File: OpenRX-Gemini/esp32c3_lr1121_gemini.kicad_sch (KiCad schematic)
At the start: 60 parts, among them T1 0900PC16J0042001E, U1 ESP32-C3FH4, U10 RFX2401C, U2 TLV75533PDQNR, U4 LR1121IMLTRT, U5 OW7EL89CENUYO3YLC-32M, U8 OW7EL89CENUYO3YLC-32M, U9 LR1121IMLTRT, X1 CJ17-400001010B20

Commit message: Gemini: copy Mono schematic as base for dual-radio build
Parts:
- removed C35, C36, C37, C40: 100nF, Capacitor_SMD:C_0201_0603Metric, symbol Device:C
- removed C38: 10pF, Capacitor_SMD:C_0201_0603Metric, symbol Device:C
- removed C39: 4.7uF, Capacitor_SMD:C_0402_1005Metric, symbol Device:C
- removed C41: 220pF, Capacitor_SMD:C_0201_0603Metric, symbol Device:C
- removed C42: 1uF, Capacitor_SMD:C_0201_0603Metric, symbol Device:C
- removed JP3: U.FL-R-SMT-1(80), OpenRX-Shared:RF-SMD_FRF05002-JSS103M, symbol OpenRX-Shared:U.FL-R-SMT-1(80)
- removed L4: 10uH, Inductor_SMD:L_0603_1608Metric, symbol Device:L
- removed R12: 220R, Resistor_SMD:R_0201_0603Metric, symbol Device:R
- removed R13, R14, R15, R16, R5, R7: 100k, Resistor_SMD:R_0201_0603Metric, symbol Device:R
- removed R8: 10k, Resistor_SMD:R_0201_0603Metric, symbol Device:R
- removed U10: RFX2401C, OpenRX-Shared:QFN-16_L3.0-W3.0-P0.50-BL-EP1.7, symbol OpenRX-Shared:RFX2401C
- removed U8: OW7EL89CENUYO3YLC-32M, OpenRX-Shared:OSC-SMD_4P-L2.0-W1.6-BL_TXC_7Z, symbol OpenRX-Shared:OW7EL89CENUYO3YLC-32M
- removed U9: LR1121IMLTRT, OpenRX-Shared:QFN-32_L5.0-W5.0-P0.50-BL-EP3.7, symbol OpenRX-Shared:LR1121IMLTRT
- added C14: 1uF, Capacitor_SMD:C_0201_0603Metric, symbol Device:C
- added C15: 220pF, Capacitor_SMD:C_0201_0603Metric, symbol Device:C
- added C16: 0.3pF, Capacitor_SMD:C_0201_0603Metric, symbol Device:C
- added C17: 100pF, Capacitor_SMD:C_0201_0603Metric, symbol Device:C
- added C18: 100nF, Capacitor_SMD:C_0201_0603Metric, symbol Device:C
- added D1: XL-1010RGBC-WS2812B, OpenRX-Shared:LED-SMD_4P-L1.0-W1.0-TL_XL-1010RGBC-WS2812B, symbol OpenRX-Shared:XL-1010RGBC-WS2812B
- added U3: TS2306A 240GF MSM 9_C2976675, OpenRX-Shared:SW-SMD_4P-L3.0-W2.0-P0.85-LS3.5, symbol OpenRX-Shared:TS2306A240GFMSM9_C2976675
- added U6: SKY13588-460LF, OpenRX-Shared:QFN-12_L2.0-W2.0-P0.50-BL-EP0.8, symbol OpenRX-Shared:SKY13588-460LF
- added U7: RFX2401C, OpenRX-Shared:QFN-16_L3.0-W3.0-P0.50-BL-EP1.7, symbol OpenRX-Shared:RFX2401C
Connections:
- net +3V3: now also C14.1, C15.1, U6.6 (VDD), U7.14 (VDD), U7.16 (VDD)
- net +5V: now also C18.1, D1.2 (VDD)
- net GND: now also C23.1, C14.2, C15.2, C16.2, C18.2, D1.3 (GND), U3.2, U6.10 (GND), U6.12 (GND), U6.13 (EP), U6.2 (GND), U6.7 (GND), U6.8 (GND), U7.1 (GND), U7.11 (GND), U7.12 (GND), U7.15 (GND), U7.17 (EP), U7.2 (GND), U7.3 (GND), U7.7 (GND), U7.8 (GND), U7.9 (GND)
- net MISO: now also U1.10 (MTDI); no longer U1.12 (MTCK)
- net MOSI: now also U1.9 (MTMS); no longer U1.13 (MTDO)
- net RXEN: now also U4.20 (DIO5), U7.6 (RXEN)
- net SCK: now also U1.12 (MTCK); no longer U1.9 (MTMS)
- net TXEN: now also U4.19 (DIO6), U7.5 (TXEN)
- net DIO8-1: now reaches U4.10 (DIO8)
- net DIO8-1: now also U6.5 (V2)
- net at USB2.1 (IN): now also U4.26 (RFIO_HF)
- net at USB2.3 (OUT): now also U7.4 (TXRX)
- net DIO7-1: now reaches U4.11 (DIO7)
- net DIO7-1: now also U6.4 (V1)
- net at U5.4 (VDD): now also C23.2, U4.3 (VTCXO); no longer C23.1
- net at T1.6 (RX), T1.8 (TX_LP), T1.9 (TX_HP): now also U6.1 (J1); no longer JP1.1 (SIG)
- net BUSY renamed BUSY1
- net BUSY2 renamed IRQ1
- net IRQ1: now also U4.9 (DIO9)
- removed net DIO1: U1.10 (MTDI), U4.9 (DIO9)
- net IRQ renamed BUTTON
- net BUTTON: now also U3.1
- net NSS renamed NSS1
- net NSS1: now also U1.13 (MTDO); no longer U1.14 (GPIO8)
- net NSS2: no longer names the net of U1.16 (GPIO10)
- net RST renamed RST1
- net RST2: no longer names the net of U1.4 (XTAL_32K_P)
- new net: C16.1, C17.2, U7.10 (ANT)
- new net: JP1.1 (SIG), U6.11 (RFC)
- new net: C17.1, U6.9 (J2)
- new net LED: D1.4 (DIN), U1.14 (GPIO8)
- no-connect marks 31 -> 22
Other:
- note removed: "interrupt (naming from lite/nano)"

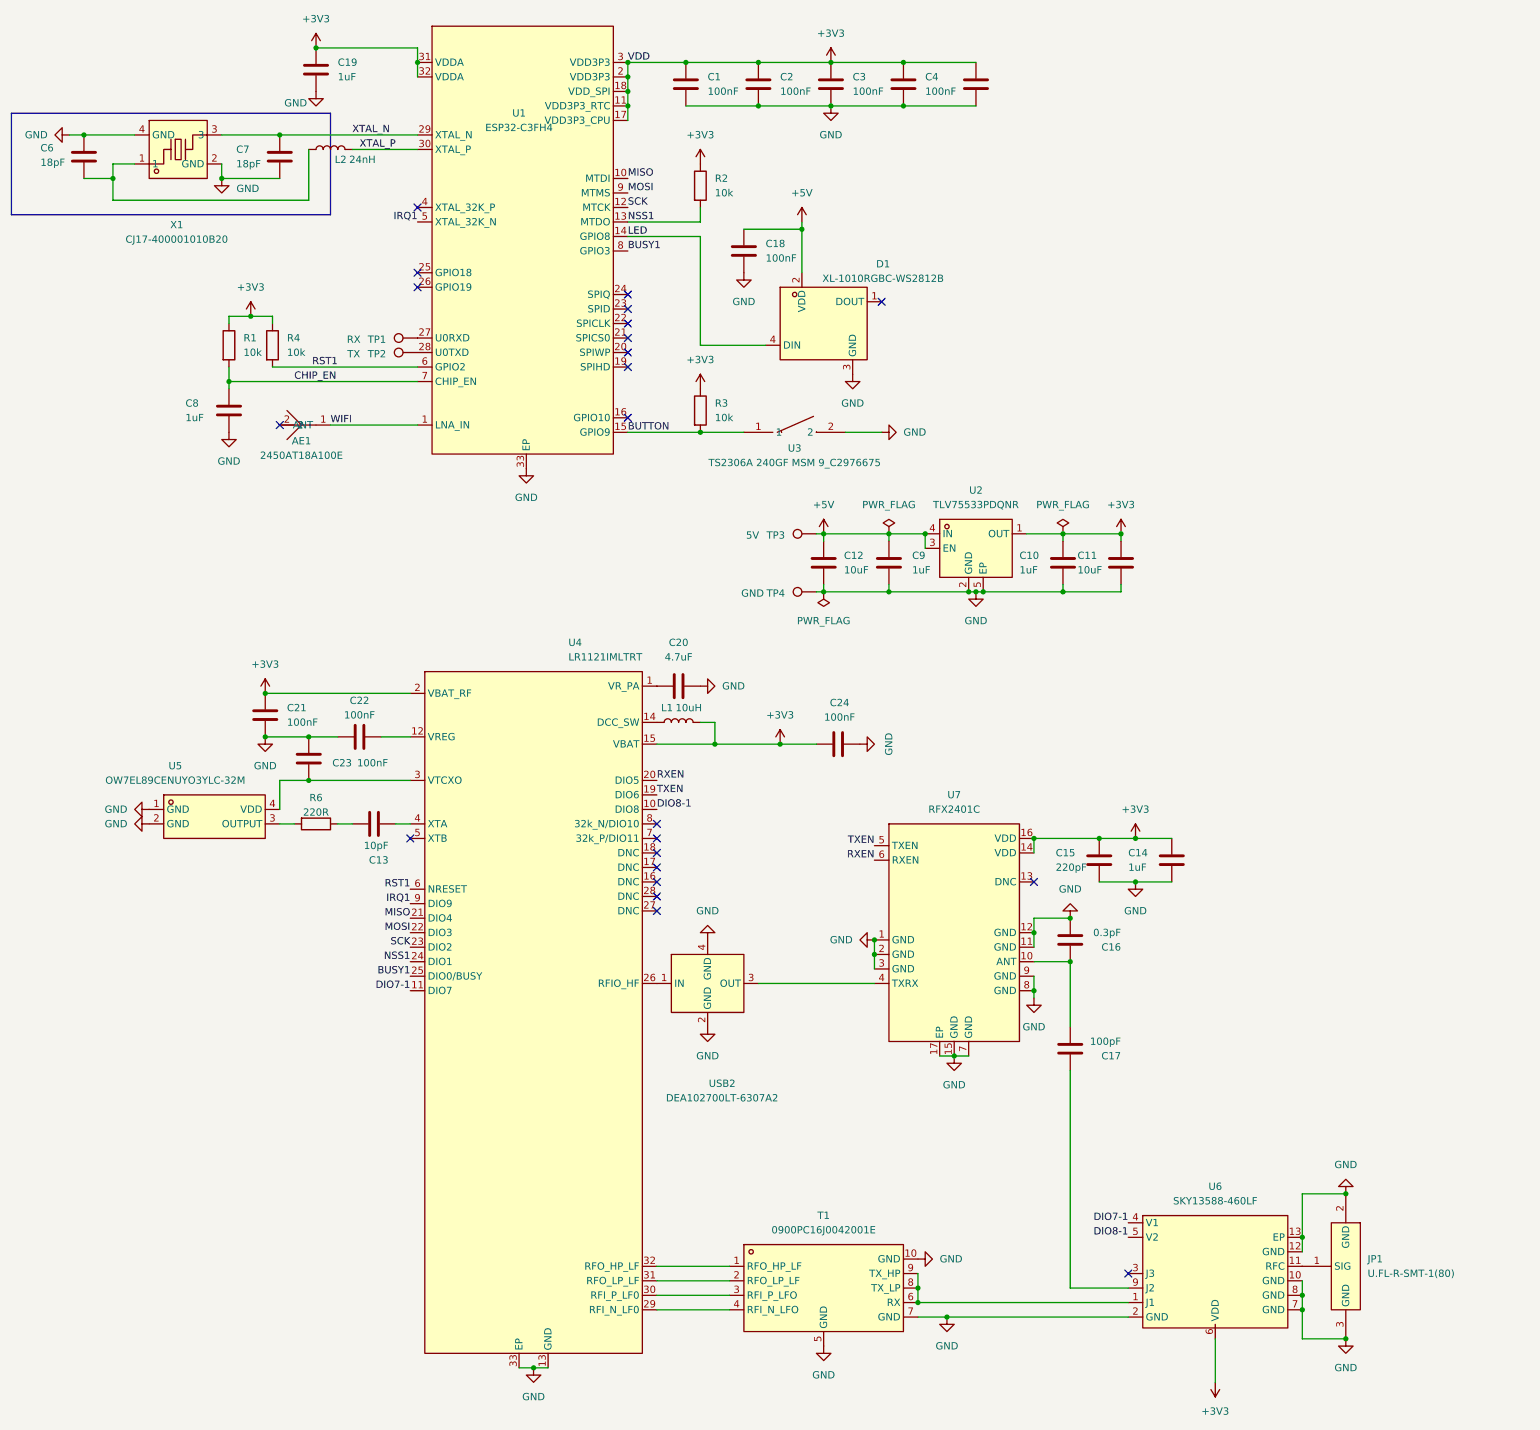
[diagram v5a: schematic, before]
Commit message: Gemini: copy Mono schematic + PCB as starting point
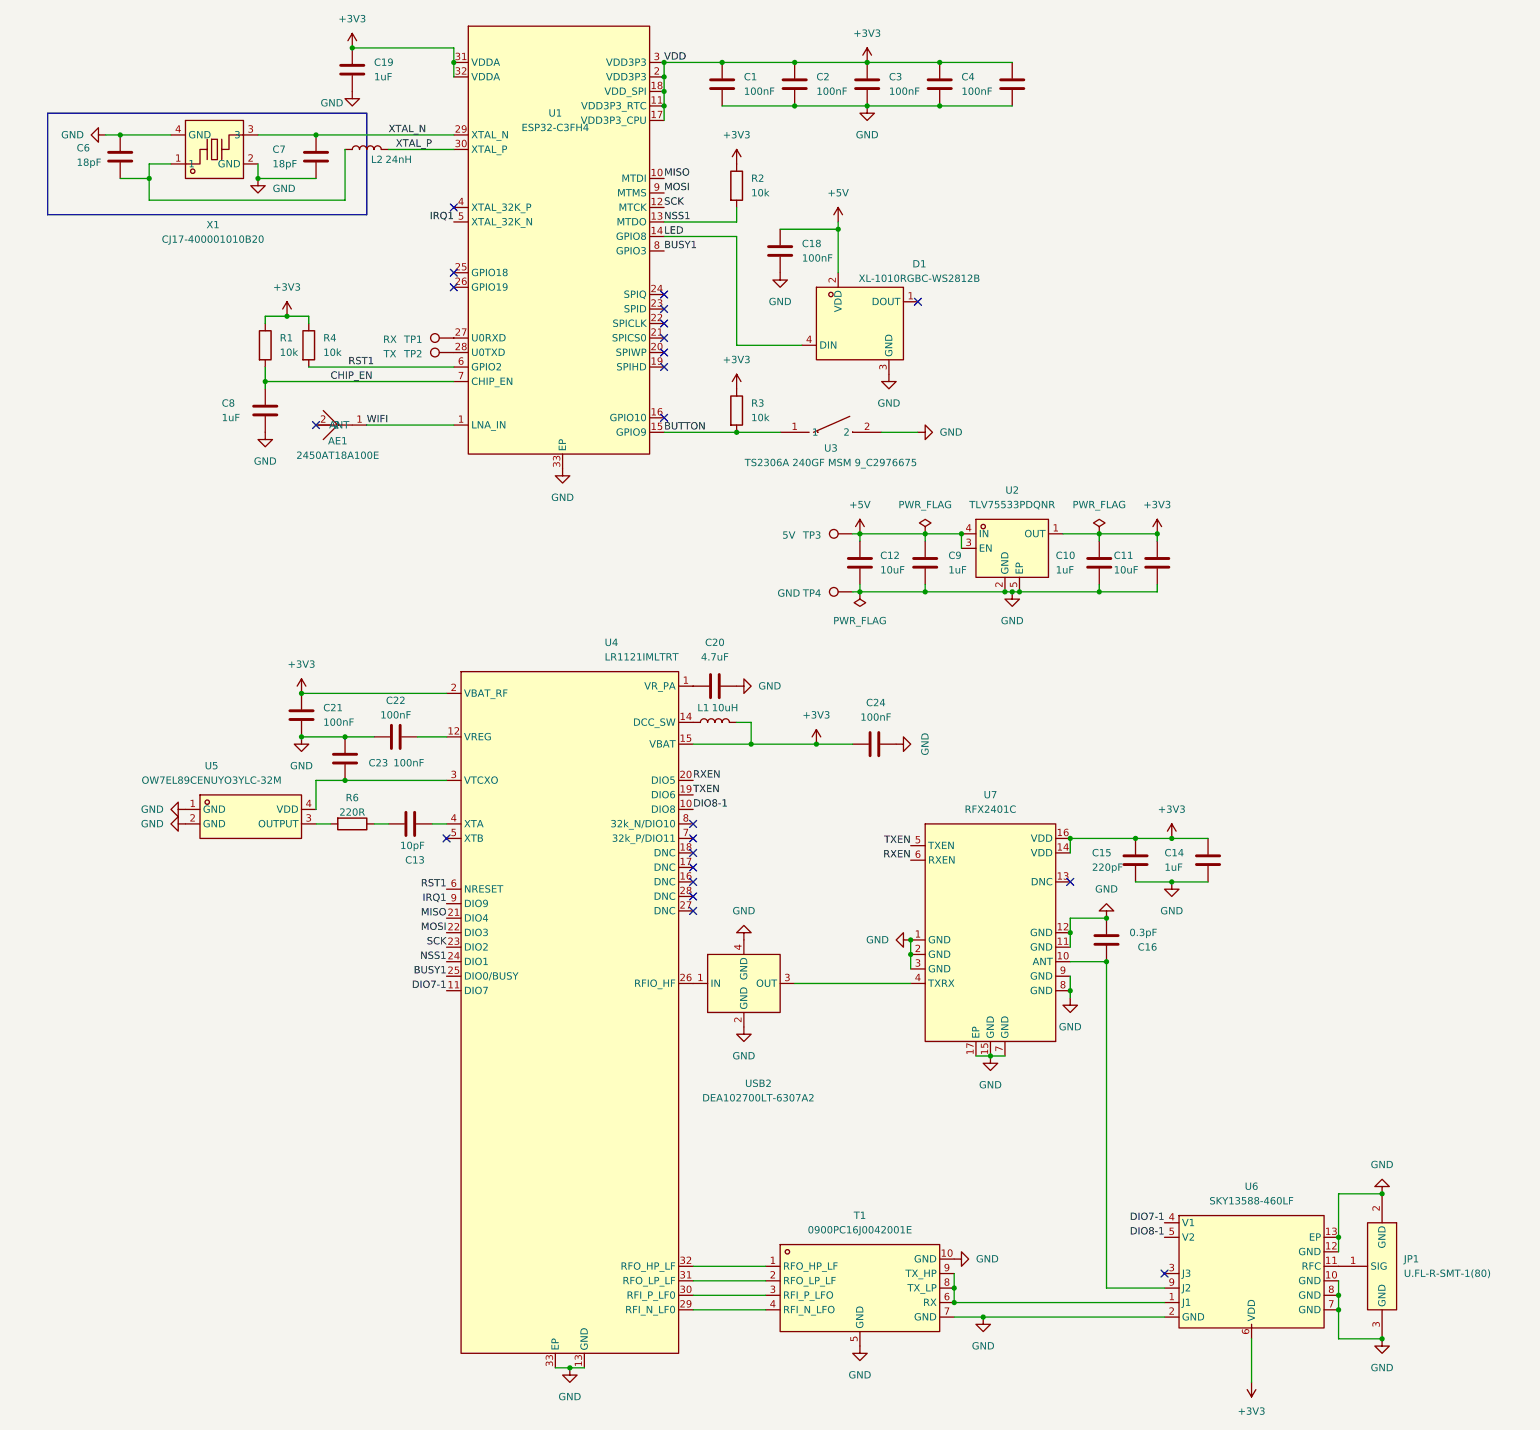
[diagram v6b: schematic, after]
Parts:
- removed C17: 100pF, Capacitor_SMD:C_0201_0603Metric, symbol Device:C
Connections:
- net at C16.1, U7.10 (ANT): now also U6.9 (J2)
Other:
- moved on the sheet: AE1, C1, C10, C11, C12, C13, C14, C15, C16, C18, C19, C2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

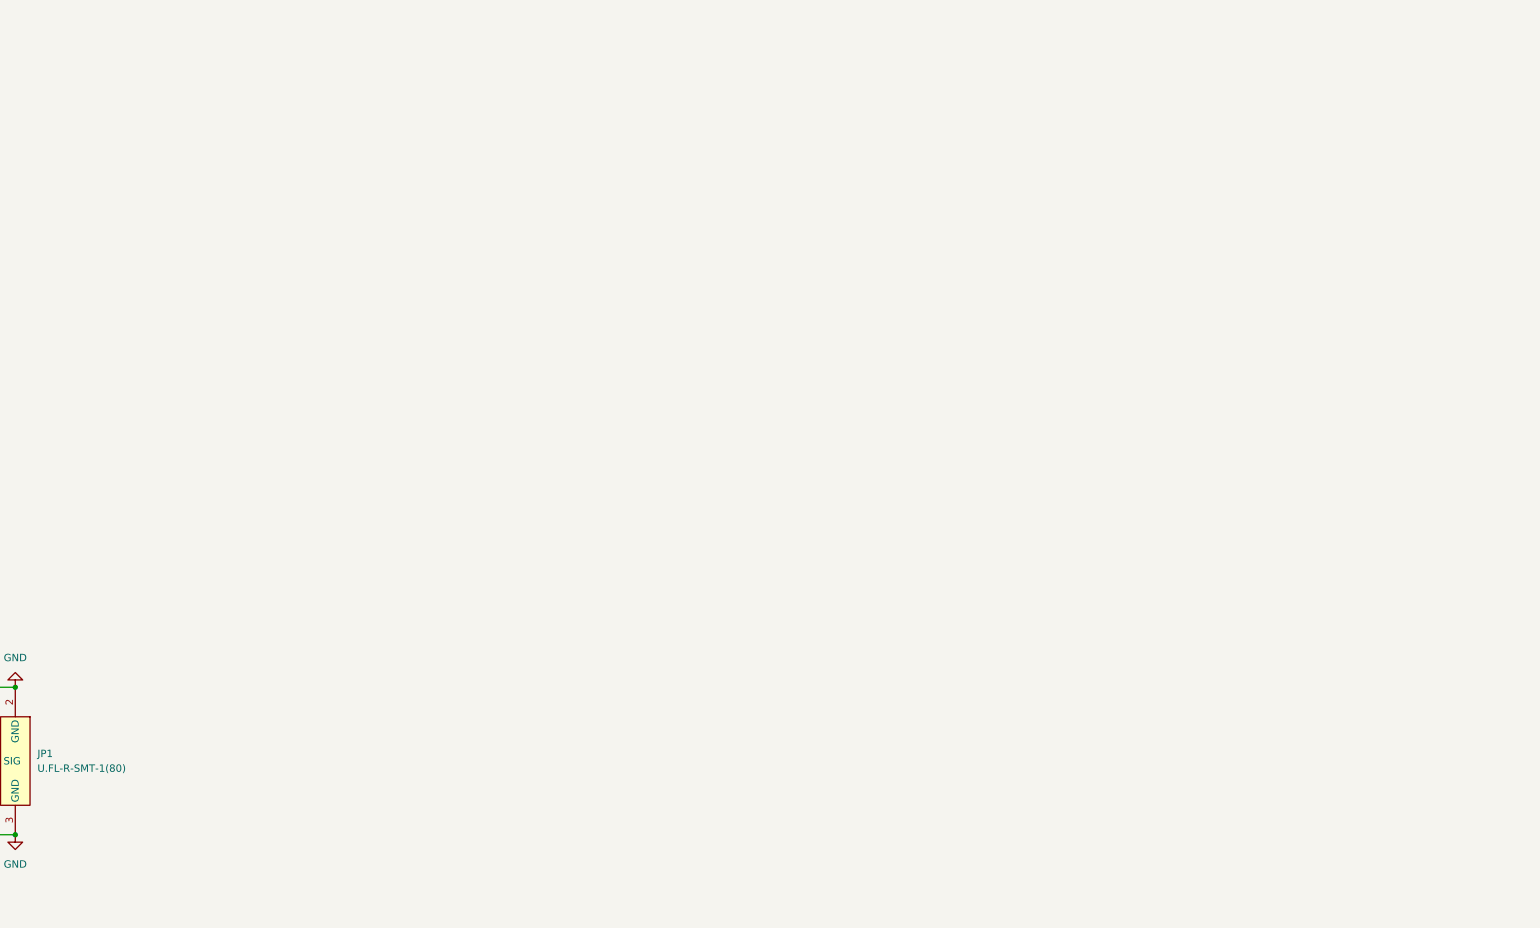
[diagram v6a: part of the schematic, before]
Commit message: Copy Gemini PCB layout to Mono
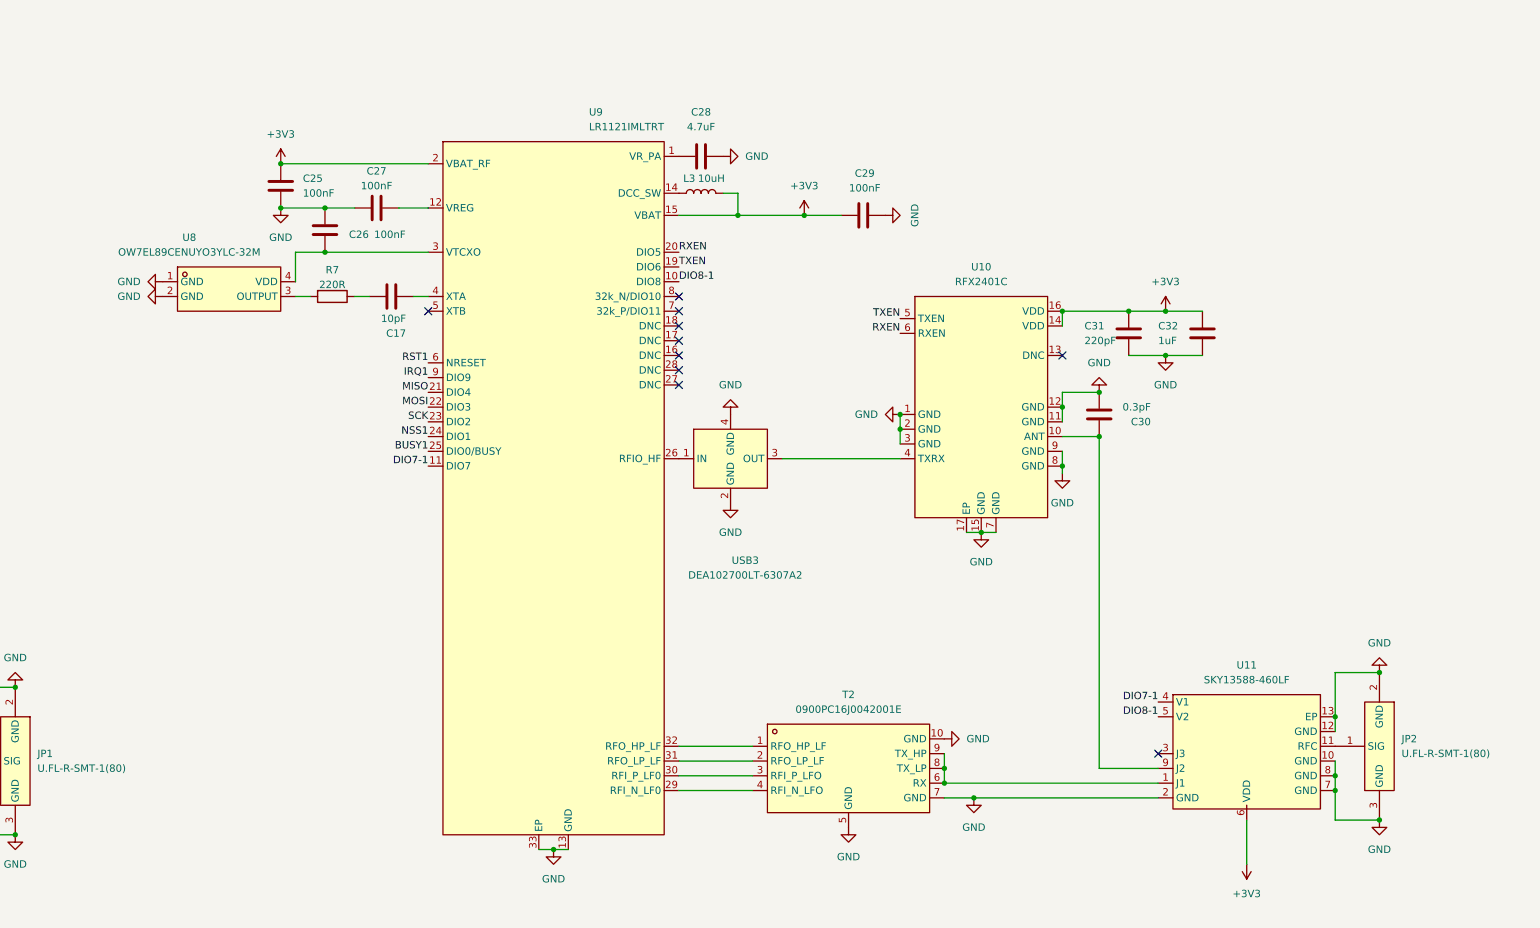
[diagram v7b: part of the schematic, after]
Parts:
- added C17: 10pF, Capacitor_SMD:C_0201_0603Metric, symbol Device:C
- added C25, C26, C27, C29: 100nF, Capacitor_SMD:C_0201_0603Metric, symbol Device:C
- added C28: 4.7uF, Capacitor_SMD:C_0402_1005Metric, symbol Device:C
- added C30: 0.3pF, Capacitor_SMD:C_0201_0603Metric, symbol Device:C
- added C31: 220pF, Capacitor_SMD:C_0201_0603Metric, symbol Device:C
- added C32: 1uF, Capacitor_SMD:C_0201_0603Metric, symbol Device:C
- added JP2: U.FL-R-SMT-1(80), OpenRX-Shared:RF-SMD_FRF05002-JSS103M, symbol OpenRX-Shared:U.FL-R-SMT-1(80)
- added L3: 10uH, Inductor_SMD:L_0603_1608Metric, symbol Device:L
- added R7: 220R, Resistor_SMD:R_0201_0603Metric, symbol Device:R
- added T2: 0900PC16J0042001E, OpenRX-Shared:FILTER-SMD_10P-L2.0-W1.6-BL, symbol OpenRX-Shared:0900PC16J0042001E
- added U10: RFX2401C, OpenRX-Shared:QFN-16_L3.0-W3.0-P0.50-BL-EP1.7, symbol OpenRX-Shared:RFX2401C
- added U11: SKY13588-460LF, OpenRX-Shared:QFN-12_L2.0-W2.0-P0.50-BL-EP0.8, symbol OpenRX-Shared:SKY13588-460LF
- added U8: OW7EL89CENUYO3YLC-32M, OpenRX-Shared:OSC-SMD_4P-L2.0-W1.6-BL_TXC_7Z, symbol OpenRX-Shared:OW7EL89CENUYO3YLC-32M
- added U9: LR1121IMLTRT, OpenRX-Shared:QFN-32_L5.0-W5.0-P0.50-BL-EP3.7, symbol OpenRX-Shared:LR1121IMLTRT
- added USB3: DEA102700LT-6307A2, OpenRX-Shared:FILTER-SMD_4P-L1.0-W0.5-L_DEA102700LT-XXX, symbol OpenRX-Shared:DEA102700LT-6307A2
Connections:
- net +3V3: now also C25.1, C29.2, C31.1, C32.1, L3.2, U10.14 (VDD), U10.16 (VDD), U11.6 (VDD), U9.15 (VBAT), U9.2 (VBAT_RF)
- net BUSY1: now also U9.25 (DIO0/BUSY)
- net DIO7-1: now also U11.4 (V1), U9.11 (DIO7)
- net DIO8-1: now also U11.5 (V2), U9.10 (DIO8)
- net GND: now also C25.2, C26.1, C27.1, C28.2, C29.1, C30.2, C31.2, C32.2, JP2.2 (GND), JP2.3 (GND), T2.10 (GND), T2.5 (GND), T2.7 (GND), U10.1 (GND), U10.11 (GND), U10.12 (GND), U10.15 (GND), U10.17 (EP), U10.2 (GND), U10.3 (GND), U10.7 (GND), U10.8 (GND), U10.9 (GND), U11.10 (GND), U11.12 (GND), U11.13 (EP), U11.2 (GND), U11.7 (GND), U11.8 (GND), U8.1 (GND), U8.2 (GND), U9.13 (GND), U9.33 (EP), USB3.2 (GND), USB3.4 (GND)
- net IRQ1: now also U9.9 (DIO9)
- net MISO: now also U9.21 (DIO4)
- net MOSI: now also U9.22 (DIO3)
- net NSS1: now also U9.24 (DIO1)
- net RST1: now also U9.6 (NRESET)
- net RXEN: now also U10.6 (RXEN), U9.20 (DIO5)
- net SCK: now also U9.23 (DIO2)
- net TXEN: now also U10.5 (TXEN), U9.19 (DIO6)
- new net: C30.1, U10.10 (ANT), U11.9 (J2)
- new net: C28.1, U9.1 (VR_PA)
- new net: C26.2, U8.4 (VDD), U9.3 (VTCXO)
- new net: T2.1 (RFO_HP_LF), U9.32 (RFO_HP_LF)
- new net: T2.2 (RFO_LP_LF), U9.31 (RFO_LP_LF)
- new net: T2.3 (RFI_P_LFO), U9.30 (RFI_P_LF0)
- new net: T2.4 (RFI_N_LFO), U9.29 (RFI_N_LF0)
- new net: T2.6 (RX), T2.8 (TX_LP), T2.9 (TX_HP), U11.1 (J1)
- new net: C17.1, R7.1
- new net: R7.2, U8.3 (OUTPUT)
- new net: C17.2, U9.4 (XTA)
- new net: L3.1, U9.14 (DCC_SW)
- new net: JP2.1 (SIG), U11.11 (RFC)
- new net: C27.2, U9.12 (VREG)
- new net: U10.4 (TXRX), USB3.3 (OUT)
- new net: U9.26 (RFIO_HF), USB3.1 (IN)
- no-connect marks 22 -> 32
